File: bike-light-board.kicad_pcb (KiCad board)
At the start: 4 copper layers, 40.2 x 69 mm, 106 parts, among them J1 KH-TYPE-C-16P, J2 S2B-PH-SM4-TB, P2 WirePad, P3 WirePad, Q1 HX2301A, Q2 L2N7002DW1T1G, Q3 HX2301A, Q4 SMD0805-20, Q5 HX2301A, SW1 SW_Push, SW2 STO-060A16AB, SW3 STO-060A16AB, U1 BRCL4054CME, U2 QMA7981, U3 ESP32-S2, U4 P25Q40H-SSH-IT, U5 ME6231A33PG, U6 M74VHC1GT126DF1G, Y1 X322540MPB4SI

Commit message: routing done
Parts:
- removed TP13: TestPoint_ICT_1mm, footprints:ICT_TestPoint_Pad_D1.00mm
- moved TP19 42.5 mm to (163.1, 80.8)
- moved TP18 28.4 mm to (152.9, 117.6)
- moved TP6 28.0 mm to (150.4, 103.6)
- moved TP5 20.8 mm to (152.9, 97.3)
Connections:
- D1 pad 1: (no net) -> Net-(D1-Pad1)
- D8 pad 2: (no net) -> Net-(D8-Pad2)
- J1 pad A8: (no net) -> Net-(J1-PadA8)
- J1 pad B8: (no net) -> Net-(J1-PadB8)
- U2 pad 11: (no net) -> Net-(U2-Pad11)
- U2 pad 4: (no net) -> Net-(U2-Pad4)
- U2 pad 6: (no net) -> Net-(U2-Pad6)
- U3 pad 17: (no net) -> Net-(U3-Pad17)
- U3 pad 18: (no net) -> Net-(U3-Pad18)
- U3 pad 19: (no net) -> Net-(U3-Pad19)
- U3 pad 21: (no net) -> Net-(U3-Pad21)
- U3 pad 22: (no net) -> Net-(U3-Pad22)
- U3 pad 28: (no net) -> Net-(U3-Pad28)
- U3 pad 29: (no net) -> Net-(U3-Pad29)
- U3 pad 39: (no net) -> Net-(U3-Pad39)
- U3 pad 40: (no net) -> Net-(U3-Pad40)
- U3 pad 43: (no net) -> /MTCK
- U3 pad 44: (no net) -> /MTDO
- U3 pad 46: (no net) -> /MTDI
- U3 pad 47: (no net) -> /MTMS
- U3 pad 50: (no net) -> Net-(U3-Pad50)
- U3 pad 55: (no net) -> Net-(U3-Pad55)
- U3 pad 6: (no net) -> Net-(U3-Pad6)
- U3 pad 7: (no net) -> Net-(U3-Pad7)
- U3 pad 8: (no net) -> Net-(U3-Pad8)
- U3 pad 9: (no net) -> Net-(U3-Pad9)
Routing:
- net +VSW: track 4.93 -> 56.0 mm, vias 4 -> 13
- net Net-(Q3-Pad3): track 0.90 -> 45.8 mm, vias 1 -> 2
- net CHRG_STAT: track 5.10 -> 49.4 mm, vias 2 -> 4
- net /VBUS: track 2.69 -> 45.4 mm, vias 1 -> 4
- net CHRG_I_MONITOR: track 2.92 -> 42.8 mm, vias 2 -> 3
- net SW_EN: track 3.21 -> 39.8 mm, vias 1 -> 2
- net EN: track 5.55 -> 41.8 mm, vias 3 -> 5
- net GND: track 44.0 -> 75.1 mm, vias 65 -> 79
- net IO0: track 1.47 -> 27.6 mm
- net ACCEL_INT: track 1.87 -> 23.5 mm
- net LIGHT_SENS: track 8.93 -> 27.9 mm
- net +3V3: track 40.8 -> 59.4 mm, vias 11 -> 18
- net Net-(D5-Pad2): track 0.00 -> 10.5 mm
- net Net-(D6-Pad2): track 0.00 -> 10.4 mm
- net Net-(D4-Pad2): track 0.00 -> 9.99 mm
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- added copper zone on B.Cu, net +3V3
- added copper zone on In1.Cu, net +3V3
- added copper zone on B.Cu, net +VSW
- added copper zone on In1.Cu, net +VSW
- added copper zone on B.Cu, net /VBAT
- added copper zone on B.Cu, net /VBUS
- added copper zone on F.Cu, net /VSUP
- added copper zone on F.Cu, net GND
- added copper zone on In1.Cu, net GND
- added copper zone on B.Cu, net Net-(J1-PadS1)

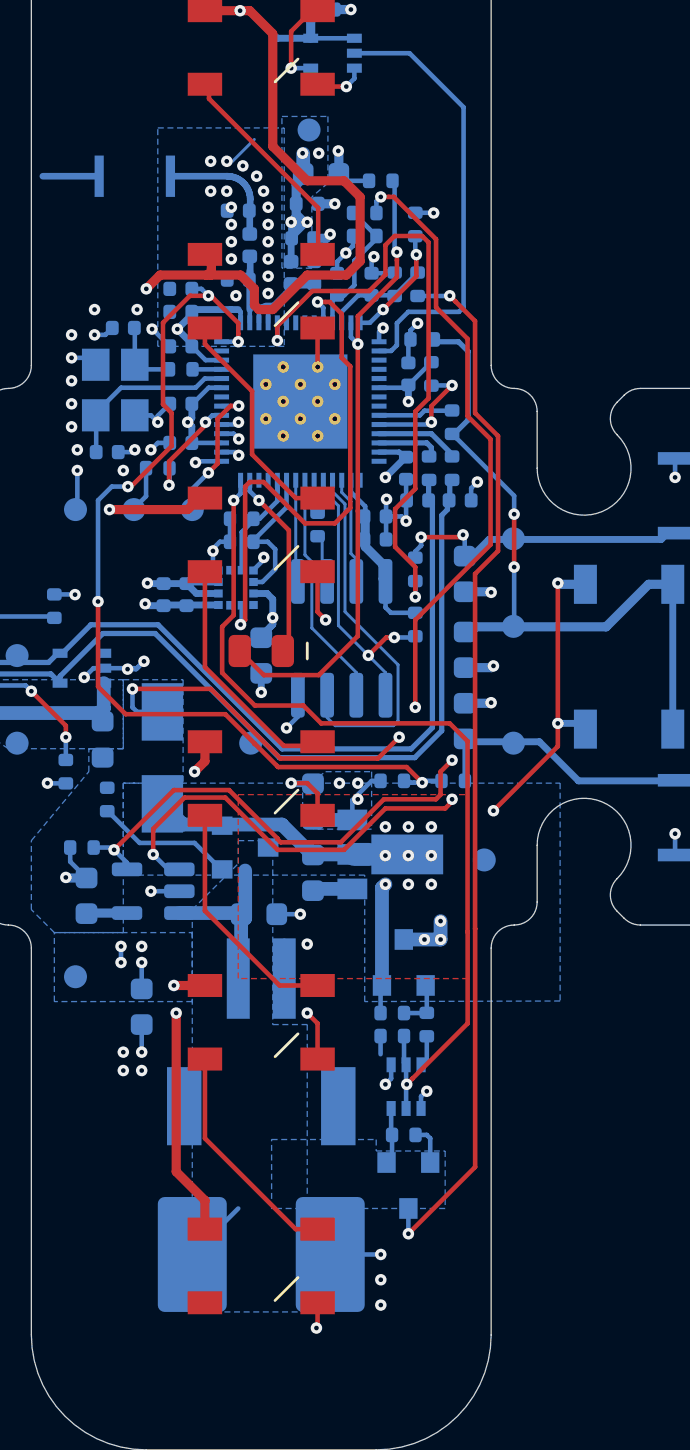
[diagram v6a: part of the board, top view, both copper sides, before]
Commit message: fix slkscreen
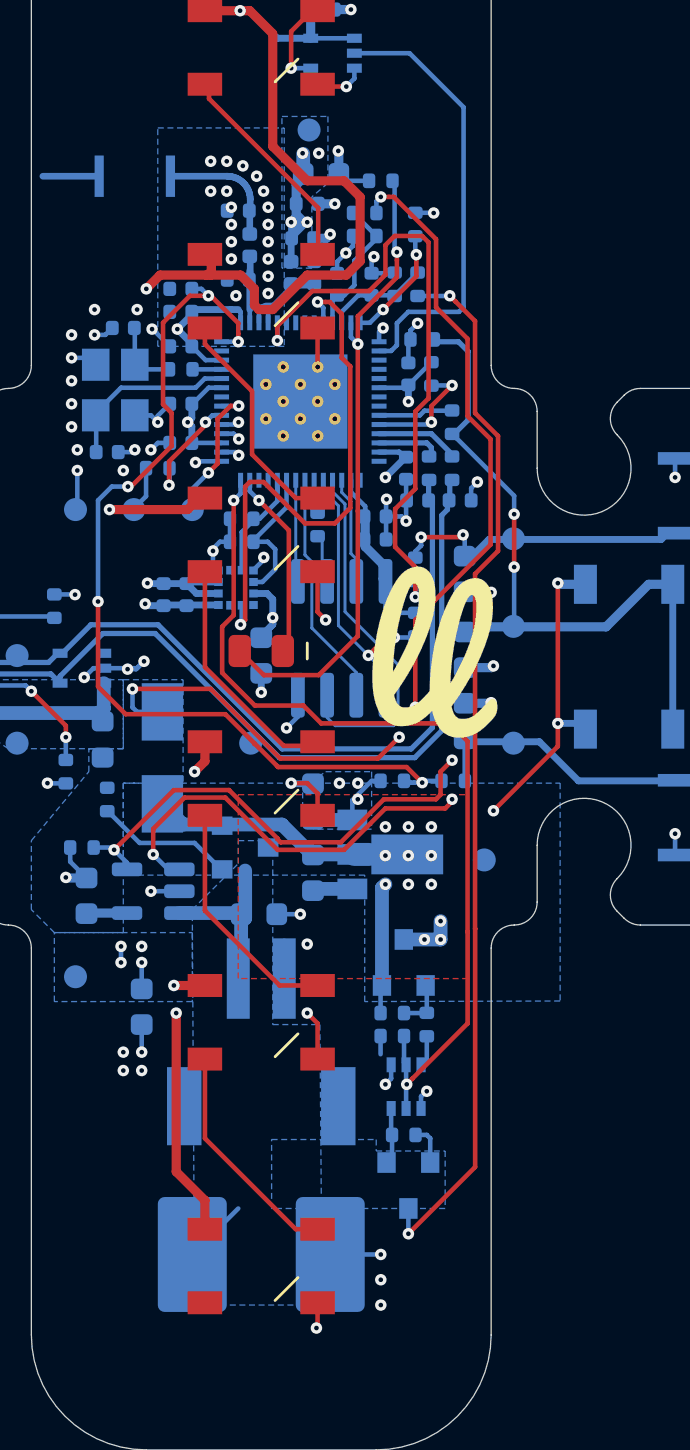
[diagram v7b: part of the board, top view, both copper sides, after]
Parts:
- added G***: LOGO, bike-light-board:Logo_Lil_Light, F.Cu at (169.9, 103.8)
- added G***: LOGO, bike-light-board:Logo_Lil_Light, F.Cu at (167.4, 103.3)
- moved LG3 14.3 mm to (154.2, 125.7)
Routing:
- net GND: track 75.1 -> 73.6 mm
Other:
- board text added: "3V3"
- board text added: "R"
- board text added: "RX"
- board text added: "TX"

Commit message: Update BOM
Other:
- board text removed: "50 ohm - 0.29 mm"
- board text removed: "BOTTOM- Signal"
- board text removed: "Layer 2- Power plane"
- board text removed: "Layer 3- Solid GND plane"
- board text removed: "STACKUP: JLC7628"
- board text removed: "TOP- power, signal"
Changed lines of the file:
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@@
   (general
     (thickness 1.6)
-    (drawings 71)
+    (drawings 55)
     (tracks 942)
     (zones 0)
@@
   (layers
     (0 F.Cu signal)
-    (1 In1.Cu signal hide)
-    (2 In2.Cu signal hide)
-    (31 B.Cu signal hide)
+    (1 In1.Cu signal)
+    (2 In2.Cu signal)
+    (31 B.Cu signal)
     (32 B.Adhes user hide)
     (33 F.Adhes user hide)
@@
     (35 F.Paste user hide)
     (36 B.SilkS user hide)
-    (37 F.SilkS user)
+    (37 F.SilkS user hide)
     (38 B.Mask user hide)
     (39 F.Mask user hide)
@@
     (45 Margin user hide)
     (46 B.CrtYd user hide)
-    (47 F.CrtYd user)
+    (47 F.CrtYd user hide)
     (48 B.Fab user hide)
     (49 F.Fab user hide)
@@
     (effects (font (size 0.8 0.8) (thickness 0.15)) (justify mirror))
   )
-  (dimension 2.5 (width 0.15) (layer Dwgs.User)
-    (gr_text "2.500 mm" (at 152.55 85.27) (layer Dwgs.User)
-      (effects (font (size 1 1) (thickness 0.15)))
-    )
-    (feature1 (pts (xy 151.3 81.87) (xy 151.3 84.556421)))
-    (feature2 (pts (xy 153.8 81.87) (xy 153.8 84.556421)))
-    (crossbar (pts (xy 153.8 83.97) (xy 151.3 83.97)))
-    (arrow1a (pts (xy 151.3 83.97) (xy 152.426504 83.383579)))
-    (arrow1b (pts (xy 151.3 83.97) (xy 152.426504 84.556421)))
-    (arrow2a (pts (xy 153.8 83.97) (xy 152.673496 83.383579)))
-    (arrow2b (pts (xy 153.8 83.97) (xy 152.673496 84.556421)))
-  )
-  (dimension 2 (width 0.15) (layer Dwgs.User)
-    (gr_text "2.000 mm" (at 158.2 79.47) (layer Dwgs.User)
-      (effects (font (size 1 1) (thickness 0.15)))
-    )
-    (feature1 (pts (xy 159.2 82.17) (xy 159.2 80.183579)))
-    (feature2 (pts (xy 157.2 82.17) (xy 157.2 80.183579)))
-    (crossbar (pts (xy 157.2 80.77) (xy 159.2 80.77)))
-    (arrow1a (pts (xy 159.2 80.77) (xy 158.073496 81.356421)))
-    (arrow1b (pts (xy 159.2 80.77) (xy 158.073496 80.183579)))
-    (arrow2a (pts (xy 157.2 80.77) (xy 158.326504 81.356421)))
-    (arrow2b (pts (xy 157.2 80.77) (xy 158.326504 80.183579)))
-  )
-  (gr_text "50 ohm - 0.29 mm" (at 234.1 149.77) (layer B.Cu)
-    (effects (font (size 1.5 1.5) (thickness 0.3)))
-  )
-  (gr_text "STACKUP: JLC7628" (at 200.6 135.77) (layer F.Cu)
-    (effects (font (size 1.5 1.5) (thickness 0.3)))
-  )
-  (dimension 69 (width 0.15) (layer Dwgs.User)
-    (gr_text "69.000 mm" (at 182.659998 104.220507 270.0000008) (layer Dwgs.User)
-      (effects (font (size 1 1) (thickness 0.15)))
-    )
-    (feature1 (pts (xy 163.899999 138.720507) (xy 181.94642 138.720507)))
-    (feature2 (pts (xy 163.899998 69.720507) (xy 181.946419 69.720507)))
-    (crossbar (pts (xy 181.359998 69.720507) (xy 181.359999 138.720507)))
-    (arrow1a (pts (xy 181.359999 138.720507) (xy 180.773578 137.594003)))
-    (arrow1b (pts (xy 181.359999 138.720507) (xy 181.94642 137.594003)))
-    (arrow2a (pts (xy 181.359998 69.720507) (xy 180.773577 70.847011)))
-    (arrow2b (pts (xy 181.359998 69.720507) (xy 181.946419 70.847011)))
-  )
-  (gr_text "Layer 2- Power plane" (at 202.6 143.77) (layer In1.Cu)
-    (effects (font (size 1.5 1.5) (thickness 0.3)))
-  )
-  (gr_text "Layer 3- Solid GND plane" (at 205 146.47) (layer In2.Cu)
-    (effects (font (size 1.5 1.5) (thickness 0.3)))
-  )
-  (gr_text "BOTTOM- Signal" (at 199.4 149.37) (layer B.Cu)
-    (effects (font (size 1.5 1.5) (thickness 0.3)))
-  )
-  (gr_text "TOP- power, signal" (at 200.9 141.17) (layer F.Cu)
-    (effects (font (size 1.5 1.5) (thickness 0.3)))
-  )
   (gr_arc (start 144.505786 93) (end 145.212893 92.292893) (angle -45) (layer Edge.Cuts) (width 0.05))
   (gr_arc (start 144.815545 93.309759) (end 145.519556 94.019947) (angle -90.25029792) (layer Edge.Cuts) (width 0.05))
@@
   (gr_line (start 170.999999 91) (end 170.999999 74.170508) (layer Edge.Cuts) (width 0.05))
   (gr_arc (start 150 93) (end 150 92) (angle -90) (layer Edge.Cuts) (width 0.05))
-  (dimension 40.159998 (width 0.15) (layer Dwgs.User)
-    (gr_text "40.160 mm" (at 160.999999 85.830508) (layer Dwgs.User)
-      (effects (font (size 1 1) (thickness 0.15)))
-    )
-    (feature1 (pts (xy 181.079998 94) (xy 181.079998 86.544087)))
-    (feature2 (pts (xy 140.92 94) (xy 140.92 86.544087)))
-    (crossbar (pts (xy 140.92 87.130508) (xy 181.079998 87.130508)))
-    (arrow1a (pts (xy 181.079998 87.130508) (xy 179.953494 87.716929)))
-    (arrow1b (pts (xy 181.079998 87.130508) (xy 179.953494 86.544087)))
-    (arrow2a (pts (xy 140.92 87.130508) (xy 142.046504 87.716929)))
-    (arrow2b (pts (xy 140.92 87.130508) (xy 142.046504 86.544087)))
-  )
-  (dimension 69 (width 0.15) (layer Dwgs.User)
-    (gr_text "69.000 mm" (at 184.759998 103.420507 270.0000008) (layer Dwgs.User)
-      (effects (font (size 1 1) (thickness 0.15)))
-    )
-    (feature1 (pts (xy 165.999999 137.920507) (xy 184.04642 137.920507)))
-    (feature2 (pts (xy 165.999998 68.920507) (xy 184.046419 68.920507)))
-    (crossbar (pts (xy 183.459998 68.920507) (xy 183.459999 137.920507)))
-    (arrow1a (pts (xy 183.459999 137.920507) (xy 182.873578 136.794003)))
-    (arrow1b (pts (xy 183.459999 137.920507) (xy 184.04642 136.794003)))
-    (arrow2a (pts (xy 183.459998 68.920507) (xy 182.873577 70.047011)))
-    (arrow2b (pts (xy 183.459998 68.920507) (xy 184.046419 70.047011)))
-  )
-  (dimension 20 (width 0.15) (layer Dwgs.User)
-    (gr_text "20.000 mm" (at 160.999999 63.330508 2.864788976e-06) (layer Dwgs.User)
-      (effects (font (size 1 1) (thickness 0.15)))
-    )
-    (feature1 (pts (xy 170.999999 74.170507) (xy 170.999998 64.044087)))
-    (feature2 (pts (xy 150.999999 74.170508) (xy 150.999998 64.044088)))
-    (crossbar (pts (xy 150.999999 64.630509) (xy 170.999999 64.630508)))
-    (arrow1a (pts (xy 170.999999 64.630508) (xy 169.873495 65.216929)))
-    (arrow1b (pts (xy 170.999999 64.630508) (xy 169.873495 64.044087)))
-    (arrow2a (pts (xy 150.999999 64.630509) (xy 152.126503 65.21693)))
-    (arrow2b (pts (xy 150.999999 64.630509) (xy 152.126503 64.044088)))
-  )
-  (gr_circle (center 163.539999 130.470508) (end 164.039999 130.470508) (layer Cmts.User) (width 0.15))
-  (gr_circle (center 158.459999 130.470508) (end 158.959999 130.470508) (layer Cmts.User) (width 0.15))
   (gr_text GND (at 163.999999 133.420508) (layer B.SilkS)
     (effects (font (size 0.8 0.8) (thickness 0.15)) (justify mirror))
@@
     (effects (font (size 0.8 0.8) (thickness 0.15)) (justify mirror))
   )
-  (gr_line (start 170.999999 90.670508) (end 170.999999 116.170508) (layer Dwgs.User) (width 0.15))
-  (gr_line (start 150.999999 90.670508) (end 150.999999 116.170508) (layer Dwgs.User) (width 0.15))
   (segment (start 153.95 82.77) (end 151.5 82.77) (width 0.29) (layer B.Cu) (net 0))
   (via (at 166.2 130.77) (size 0.5) (drill 0.2) (layers F.Cu B.Cu) (net 1))
